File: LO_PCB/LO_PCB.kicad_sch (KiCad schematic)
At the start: 2 parts, among them U1 LMX2582RHAR

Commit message: some more stuff put in
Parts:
- added C1, C4, C6, C9: 1uF, symbol Device:C
- added C10, C11, C5, C7, C8: 10uF, symbol Device:C
- added C12, C2, C3: 0.1uF, symbol Device:C
- added C16, C17, C18: 100pF, symbol Device:C
- added J1: OSCinP, symbol Connector:Conn_Coaxial
- added J2: OSCinM, symbol Connector:Conn_Coaxial
- added J5: RFoutBP, symbol Connector:Conn_Coaxial
- added J6: RFoutBM, symbol Connector:Conn_Coaxial
- added R1: 10, symbol Device:R
- added R13, R14, R15, R16: 49.9, symbol Device:R
- added R2, R3, R4, R7, R8: 18, symbol Device:R
- added R5, R6: 68, symbol Device:R
- added U2: TPS7A9101DSKT, Snapeda:DSK0010A, symbol Snapeda:TPS7A9101DSKT
- added U3, U4: PE42424A-Z, Snapeda:DFN6_1P5X1P5-0P5_PSM, symbol Snapeda:PE42424A-Z
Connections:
- net GND: now also C1.2, C10.1, C11.2, C12.2, C17.1, C4.1, C5.1, C6.1, C7.1, C8.1, C9.1, J1.2 (Ext), J2.2 (Ext), J5.2 (Ext), J6.2 (Ext), R15.2, R16.2, R5.2, R6.2, U2.11 (PAD), U2.4 (GND)
- net at XTAL1.3 (OUTPUT): now also R2.1
- net at XTAL1.4 (VCC): now also C1.1, R1.2
- net at U1.10 (VREGIN): now also C4.2
- net at U1.18 (RFOUTBM): now also C18.2, R14.2
- net at U1.19 (RFOUTBP): now also C16.2, R13.1
- net at U1.27 (VBIASVCO2): now also C9.2
- net at U1.29 (VREFVCO2): now also C7.2
- net at U1.3 (VBIASVCO): now also C8.2
- net at U1.33 (VBIASVARAC): now also C10.2
- net at U1.36 (VREFVCO): now also C5.2
- net at U1.38 (VREGVCO): now also C6.2
- net at U1.8 (OSCINP): now also C2.2
- net at U1.9 (OSCINM): now also C3.2
- new net: R4.2, R6.1, R8.1
- new net: C2.1, R7.2
- new net: C3.1, R8.2
- new net: J1.1 (In), R3.1
- new net: C18.1, J6.1 (In), R16.1
- new net: J2.1 (In), R4.1
- new net: C16.1, J5.1 (In), R15.1
- new net: R2.2, R3.2, R5.1, R7.1
- new net: C11.1, U2.10 (IN), U2.6 (SS_CTRL), U2.7 (EN), U2.9 (IN)
- new net: U2.1 (OUT), U2.2 (OUT)
- new net: C12.1, U2.8 (NR_SS)
- new net VCC: R1.1
- new net VccRF: C17.2, R13.2, R14.1
- no-connect marks 8 -> 5
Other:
- note added: "External Input Reference SMA"
- note added: "On-Board Oscillator 100 MHz, 25ppm"
- note added: "Reference Clock"
- moved on the sheet: U1

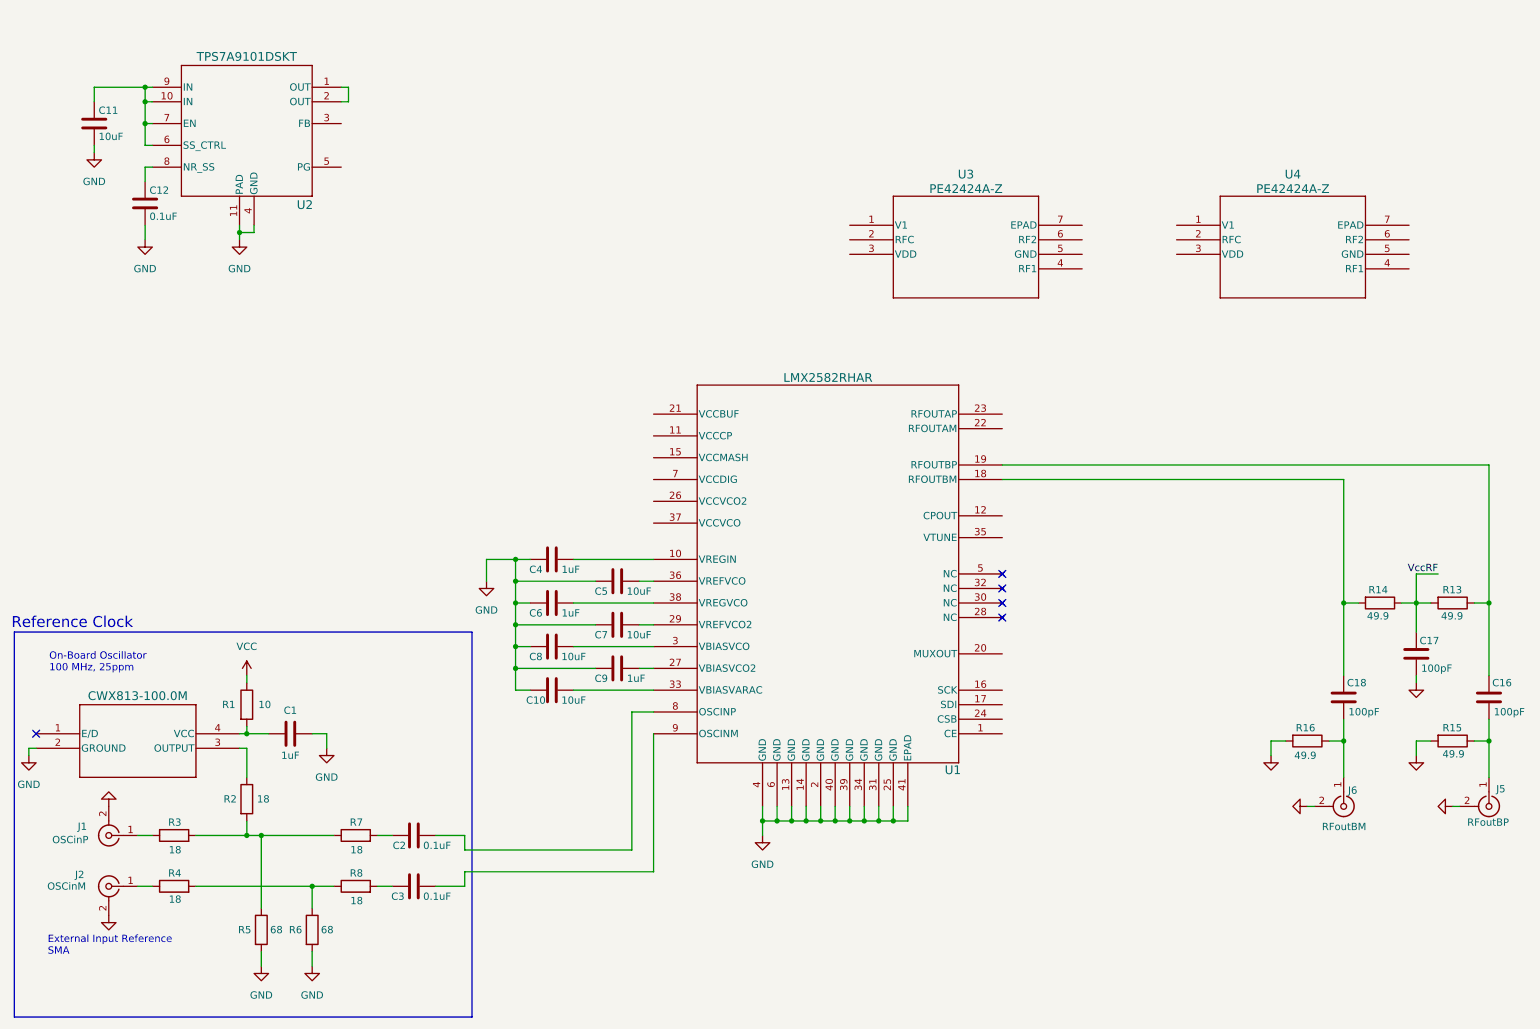
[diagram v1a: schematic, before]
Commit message: added power section, headers for SPI, loop filter and a bit of cleanup
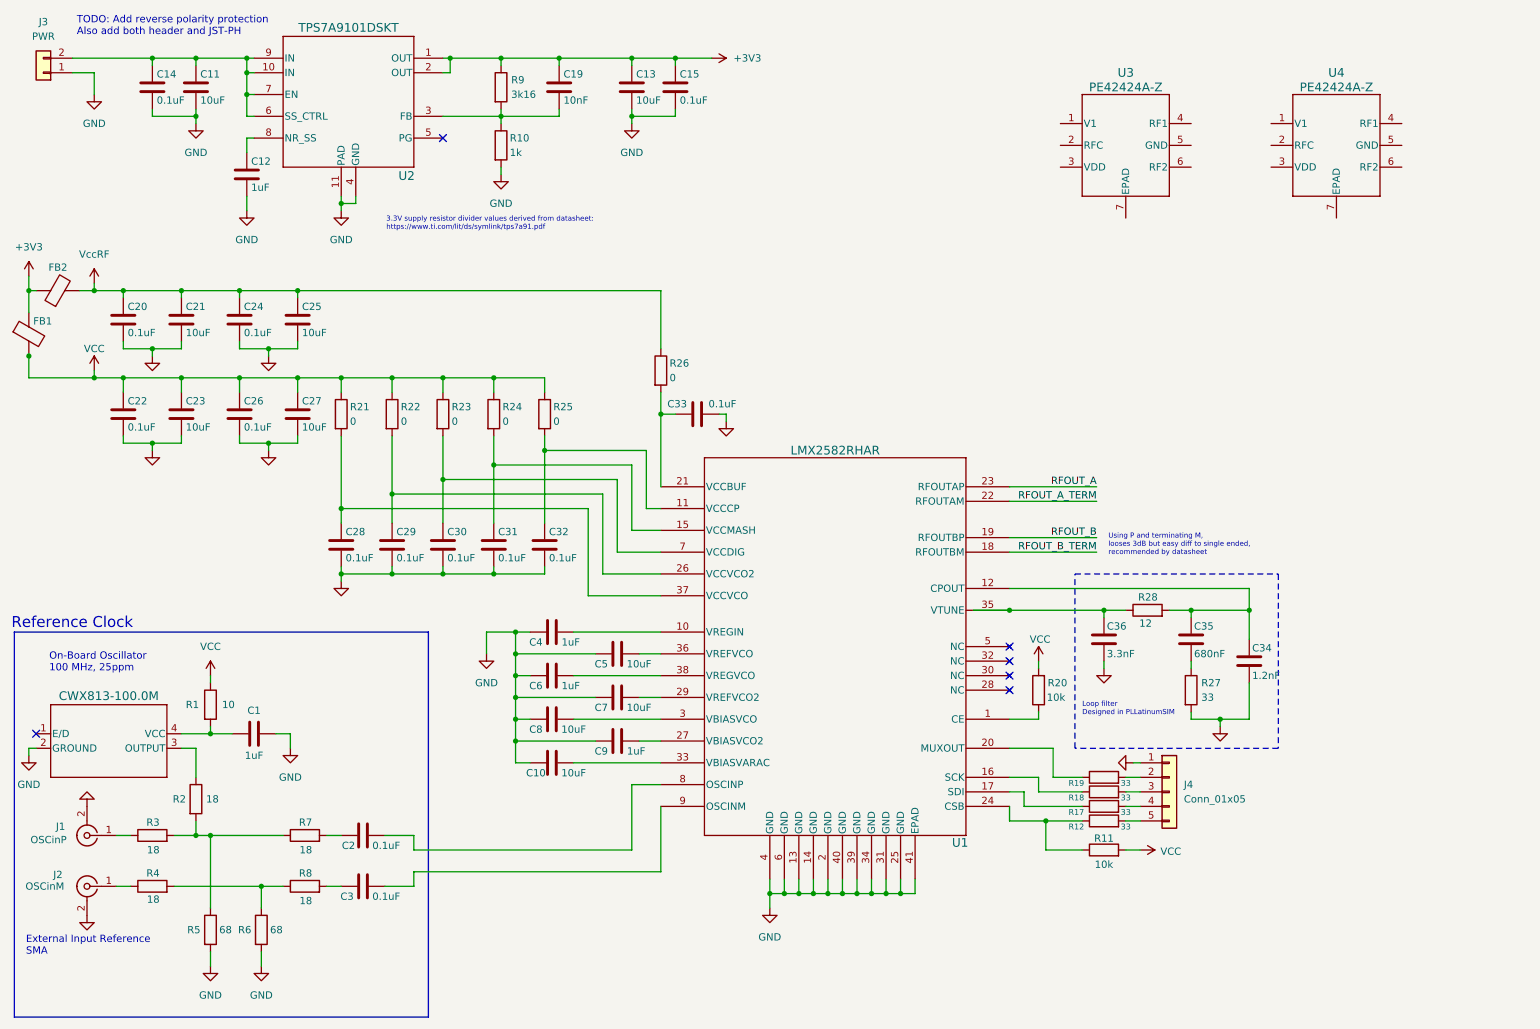
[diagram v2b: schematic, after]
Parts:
- removed C16, C17, C18: 100pF, symbol Device:C
- removed J5: RFoutBP, symbol Connector:Conn_Coaxial
- removed J6: RFoutBM, symbol Connector:Conn_Coaxial
- removed R13, R14, R15, R16: 49.9, symbol Device:R
- added C13, C21, C23, C25, C27: 10uF, symbol Device:C
- added C14, C15, C20, C22, C24, C26, C28, C29, C30, C31, C32, C33: 0.1uF, symbol Device:C
- added C19: 10nF, symbol Device:C
- added C34: 1.2nF, symbol Device:C
- added C35: 680nF, symbol Device:C
- added C36: 3.3nF, symbol Device:C
- added FB1, FB2: (no value), symbol Device:FerriteBead
- added J3: PWR, Connector_PinHeader_2.54mm:PinHeader_1x02_P2.54mm_Vertical, symbol Connector_Generic:Conn_01x02
- added J4: Conn_01x05, symbol Connector_Generic:Conn_01x05
- added R10: 1k, symbol Device:R
- added R11, R20: 10k, symbol Device:R
- added R12, R17, R18, R19, R27: 33, symbol Device:R
- added R21, R22, R23, R24, R25, R26: 0, symbol Device:R
- added R28: 12, symbol Device:R
- added R9: 3k16, symbol Device:R
- C12: value 0.1uF -> 1uF
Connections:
- net GND: now also C13.2, C14.2, C15.2, C20.2, C21.2, C22.2, C23.2, C24.2, C25.2, C26.2, C27.2, C28.2, C29.2, C30.2, C31.2, C32.2, C33.2, C34.2, C36.2, J3.1 (Pin_1), J4.1 (Pin_1), R10.2, R27.2
- net VCC: now also C22.1, C23.1, C26.1, C27.1, FB1.2, R11.2, R20.2, R21.1, R22.1, R23.1, R24.1, R25.1
- net VccRF: now also C20.1, C21.1, C24.1, C25.1, FB2.2, R26.1
- net RFOUT_B_TERM: now reaches U1.18 (RFOUTBM)
- net RFOUT_B: now reaches U1.19 (RFOUTBP)
- net at C11.1, U2.10 (IN), U2.6 (SS_CTRL)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: now also C14.1, J3.2 (Pin_2)
- net at U1.1 (CE): now also R20.1
- net at U1.11 (VCCCP): now also C32.1, R25.2
- net at U1.12 (CPOUT): now also C34.1, C35.1, R28.2
- net at U1.15 (VCCMASH): now also C31.1, R24.2
- net at U1.16 (SCK): now also R18.1
- net at U1.17 (SDI): now also R17.1
- net at U1.20 (MUXOUT): now also R19.1
- net at U1.21 (VCCBUF): now also C33.1, R26.2
- net RFOUT_A_TERM: now reaches U1.22 (RFOUTAM)
- net RFOUT_A: now reaches U1.23 (RFOUTAP)
- net at U1.24 (CSB): now also R11.1, R12.1
- net at U1.26 (VCCVCO2): now also C29.1, R22.2
- net at U1.35 (VTUNE): now also C36.1, R28.1
- net at U1.37 (VCCVCO): now also C28.1, R21.2
- net at U1.7 (VCCDIG): now also C30.1, R23.2
- net +3V3: now reaches U2.1 (OUT), U2.2 (OUT)
- net +3V3: now also C13.1, C15.1, C19.1, FB1.1, FB2.1, R9.1
- net at U2.3 (FB): now also C19.2, R10.1, R9.2
- new net: J4.4 (Pin_4), R17.2
- new net: J4.5 (Pin_5), R12.2
- new net: J4.2 (Pin_2), R19.2
- new net: J4.3 (Pin_3), R18.2
- new net: C35.2, R27.1
- no-connect marks 5 -> 6
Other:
- note added: "3.3V supply resistor divider values derived from datasheet: https://www.ti.com/lit/ds/symlink/tps7a91.pdf"
- note added: "Loop filter Designed in PLLatinumSIM"
- note added: "TODO: Add reverse polarity protection Also add both header and JST-PH"
- note added: "Using P and terminating M, looses 3dB but easy diff to single ended, recommended by datasheet"
- title: (none) -> PLL Board
- moved on the sheet: C1, C10, C11, C12, C2, C3, C4, C5, C6, C7, C8, C9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

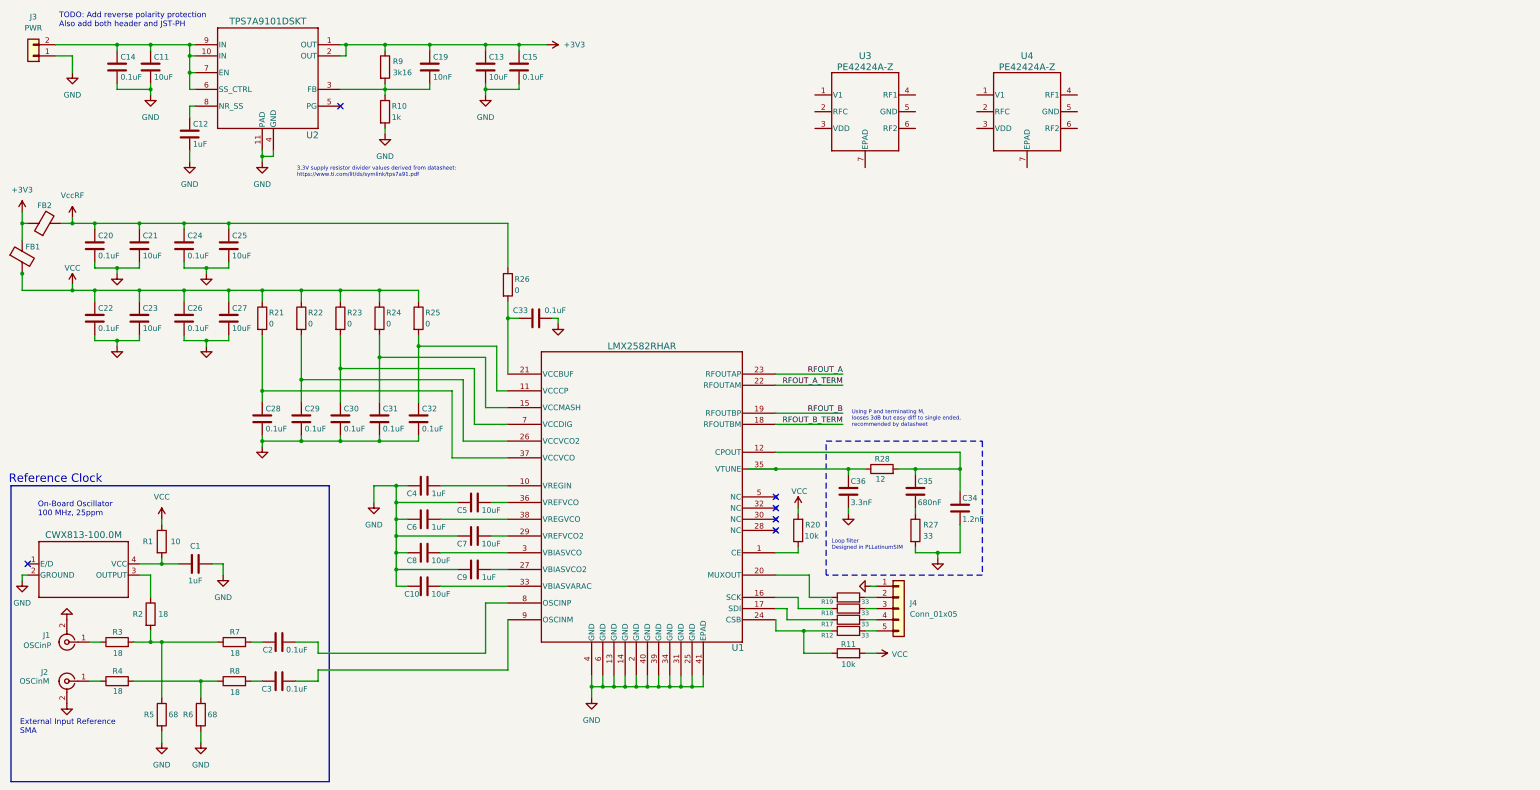
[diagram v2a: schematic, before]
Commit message: terminated differential PLL output to single ended and started work on switched filter bank design for LO output
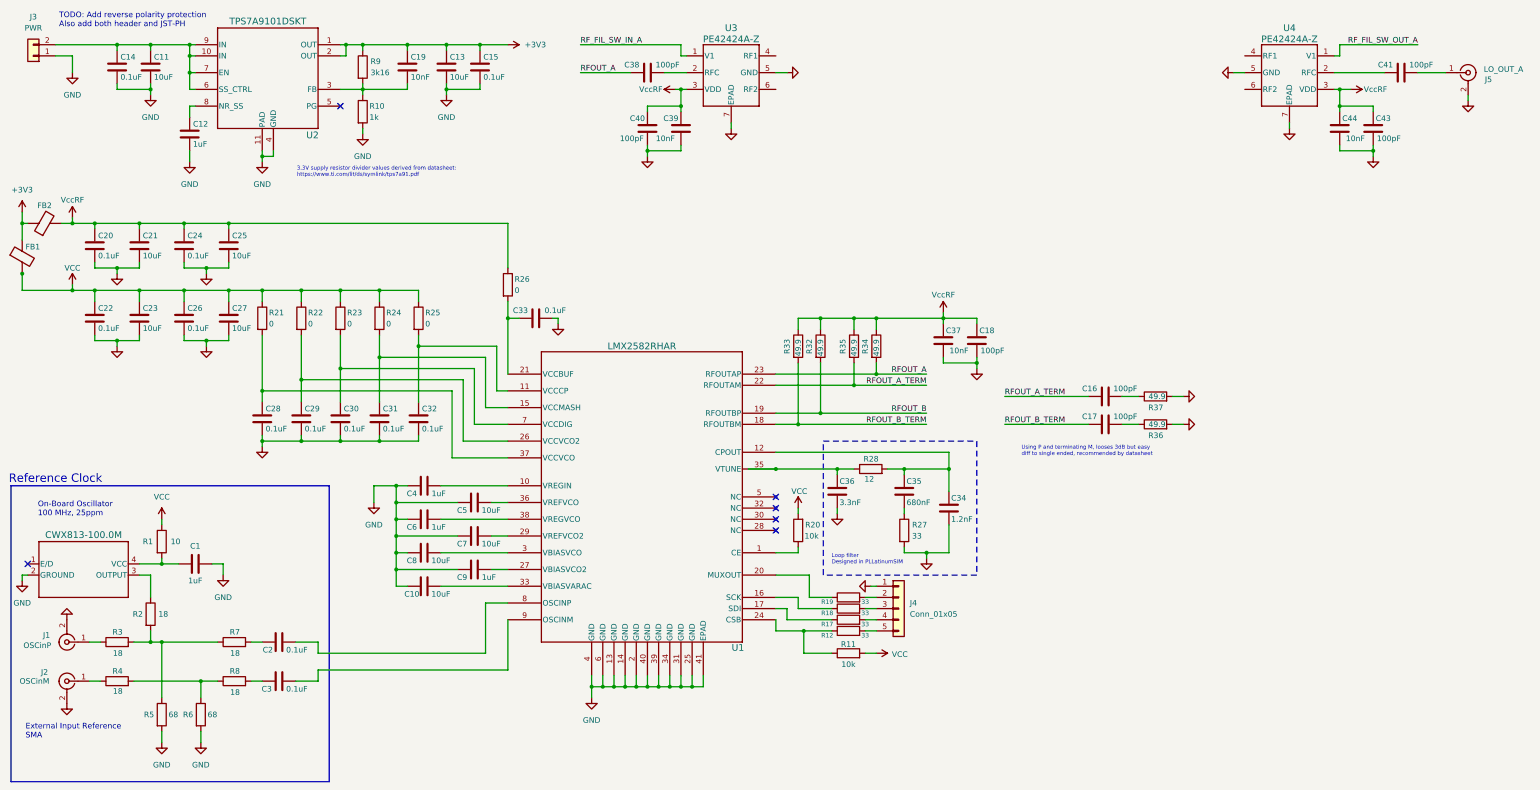
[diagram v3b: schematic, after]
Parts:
- added C16, C17, C18, C38, C40, C41, C43: 100pF, symbol Device:C
- added C37, C39, C44: 10nF, symbol Device:C
- added J5: LO_OUT_A, symbol Connector:Conn_Coaxial
- added R32, R33, R34, R35, R36, R37: 49.9, symbol Device:R
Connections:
- net GND: now also U3.5 (GND), U3.7 (EPAD), U4.5 (GND), U4.7 (EPAD), C18.1, C37.1, C39.1, C40.1, C43.1, C44.1, J5.2 (Ext), R36.2, R37.2
- net RFOUT_A: now also C38.1, R34.2
- net RFOUT_A_TERM: now also C16.1, R35.2
- net RFOUT_B: now also R32.2
- net RFOUT_B_TERM: now also C17.1, R33.2
- net VccRF: now also U3.3 (VDD), U4.3 (VDD), C18.2, C37.2, C39.2, C40.2, C43.2, C44.2, R32.1, R33.1, R34.1, R35.1
- net RF_FIL_SW_OUT_A: now reaches U4.1 (V1)
- net at U4.2 (RFC): now also C41.1
- net RF_FIL_SW_IN_A: now reaches U3.1 (V1)
- net at U3.2 (RFC): now also C38.2
- new net: C41.2, J5.1 (In)
- new net: C16.2, R37.1
- new net: C17.2, R36.1
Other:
- moved on the sheet: C13, C15, C19, C34, C35, C36, R10, R27, R28, R9, U3

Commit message: finished schematic for PLL?
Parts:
- removed FB1, FB2: (no value), symbol Device:FerriteBead
- removed J4: Conn_01x05, symbol Connector_Generic:Conn_01x05
- added C42, C46, C53, C57: 3.6pF, symbol Device:C
- added C45, C55: 6.2pF, symbol Device:C
- added C47, C49, C54, C58: 1.2pF, symbol Device:C
- added C48, C56: 2pF, symbol Device:C
- added C50, C51, C60, C61: 100pF, symbol Device:C
- added C52, C59: 10nF, symbol Device:C
- added J4: Conn_01x08, symbol Connector_Generic:Conn_01x08
- added J6: LO_OUT_A, symbol Connector:Conn_Coaxial
- added L1, L2, L5, L7: 10nH, symbol Device:L
- added L3, L4, L6, L8: 3.6nH, symbol Device:L
- added Q1: AO3401A, Snapeda:SOT-23-3L_AOS-L, symbol Transistor_FET:Q_PMOS_GSD
- added R13: 100k, symbol Device:R
- added R29, R30: 0, symbol Device:R
- added U5, U6: PE42424A-Z, Snapeda:DFN6_1P5X1P5-0P5_PSM, symbol Snapeda:PE42424A-Z
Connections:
- net +3V3: now also R29.1, R30.1
- net GND: now also C42.2, C45.2, C46.2, C47.2, C48.2, C49.2, C51.1, C52.1, C53.2, C54.2, C55.2, C56.2, C57.2, C58.2, C59.1, C60.1, J4.1 (Pin_1), J4.8 (Pin_8), J6.2 (Ext), R13.2, U5.5 (GND), U5.7 (EPAD), U6.5 (GND), U6.7 (EPAD)
- net RFOUT_B: now also C50.1
- net VCC: now also R29.2
- net VccRF: now also C51.2, C52.2, C59.2, C60.2, R30.2, U5.3 (VDD), U6.3 (VDD)
- net at R17.2: now also J4.6 (Pin_6)
- net at R12.2: now also J4.7 (Pin_7)
- net at C11.1, C14.1, U2.10 (IN)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: now also Q1.2 (S); no longer J3.2 (Pin_2)
- net at R19.2: now also J4.4 (Pin_4)
- net at R18.2: now also J4.5 (Pin_5)
- net at U4.4 (RF2): now also C49.1, L4.2
- net at U4.6 (RF1): now also C46.1, L2.2
- net at U3.4 (RF2): now also C47.1, L3.1
- net at U3.6 (RF1): now also C42.1, L1.1
- net RF_FIL_SW_IN_A renamed RF_FIL_SW_IN
- net RF_FIL_SW_IN: now also U5.1 (V1)
- net RF_FIL_SW_OUT_A renamed RF_FIL_SW_OUT
- net RF_FIL_SW_OUT: now also U6.1 (V1)
- new net: C48.1, L3.2, L4.1
- new net: C45.1, L1.2, L2.1
- new net: C56.1, L6.2, L8.1
- new net: C57.1, L7.2, U6.4 (RF1)
- new net: J3.2 (Pin_2), Q1.3 (D)
- new net: C61.1, U6.2 (RFC)
- new net: C61.2, J6.1 (In)
- new net: C54.1, L6.1, U5.6 (RF2)
- new net: C58.1, L8.2, U6.6 (RF2)
- new net: C55.1, L5.2, L7.1
- new net: C50.2, U5.2 (RFC)
- new net: C53.1, L5.1, U5.4 (RF1)
- new net: Q1.1 (G), R13.1
- new net PF_FIL_SW_IN: J4.3 (Pin_3)
- new net PF_FIL_SW_OUT: J4.2 (Pin_2)
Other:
- note added: "Output A Switched Filter Bank of 5th order Chebychev Lowpass filters: Upper path: 1050 MHz cutoff Lower path: 3000 MHz cutoff"
- note added: "Output B Switched Filter Bank of 5th order Chebychev Lowpass filters: Upper path: 1050 MHz cutoff Lower path: 3000 MHz cutoff"
- note added: "Reverse polarit protection"
- note added: "Since the LMX2582 only cannot output arbitrary frequencies independently on port A and B, I've decided that they will always output the same frequency (simplifies design). Therefore, the filter bank selection signal will be shared between port A and B, simplifying interface. Note: SW_IN and SW_OUT have to be logically inverted for the design to work. It was deemed that it was simpler to just addr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"
- note removed: "TODO: Add reverse polarity protection Also add both header and JST-PH"
- moved on the sheet: C1, C10, C11, C12, C13, C14, C15, C16, C17, C18, C19, C2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
